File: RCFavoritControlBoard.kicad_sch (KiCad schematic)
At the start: 30 parts, among them J1 Screw_Terminal_01x02, J2 Screw_Terminal_01x02, J3 Conn_01x03_Pin, U1 SY8303, U2 TPS7A20xxxPDBVR, U3 DRV8833PWP, U4 XIAO-ESP32-S3-SMD

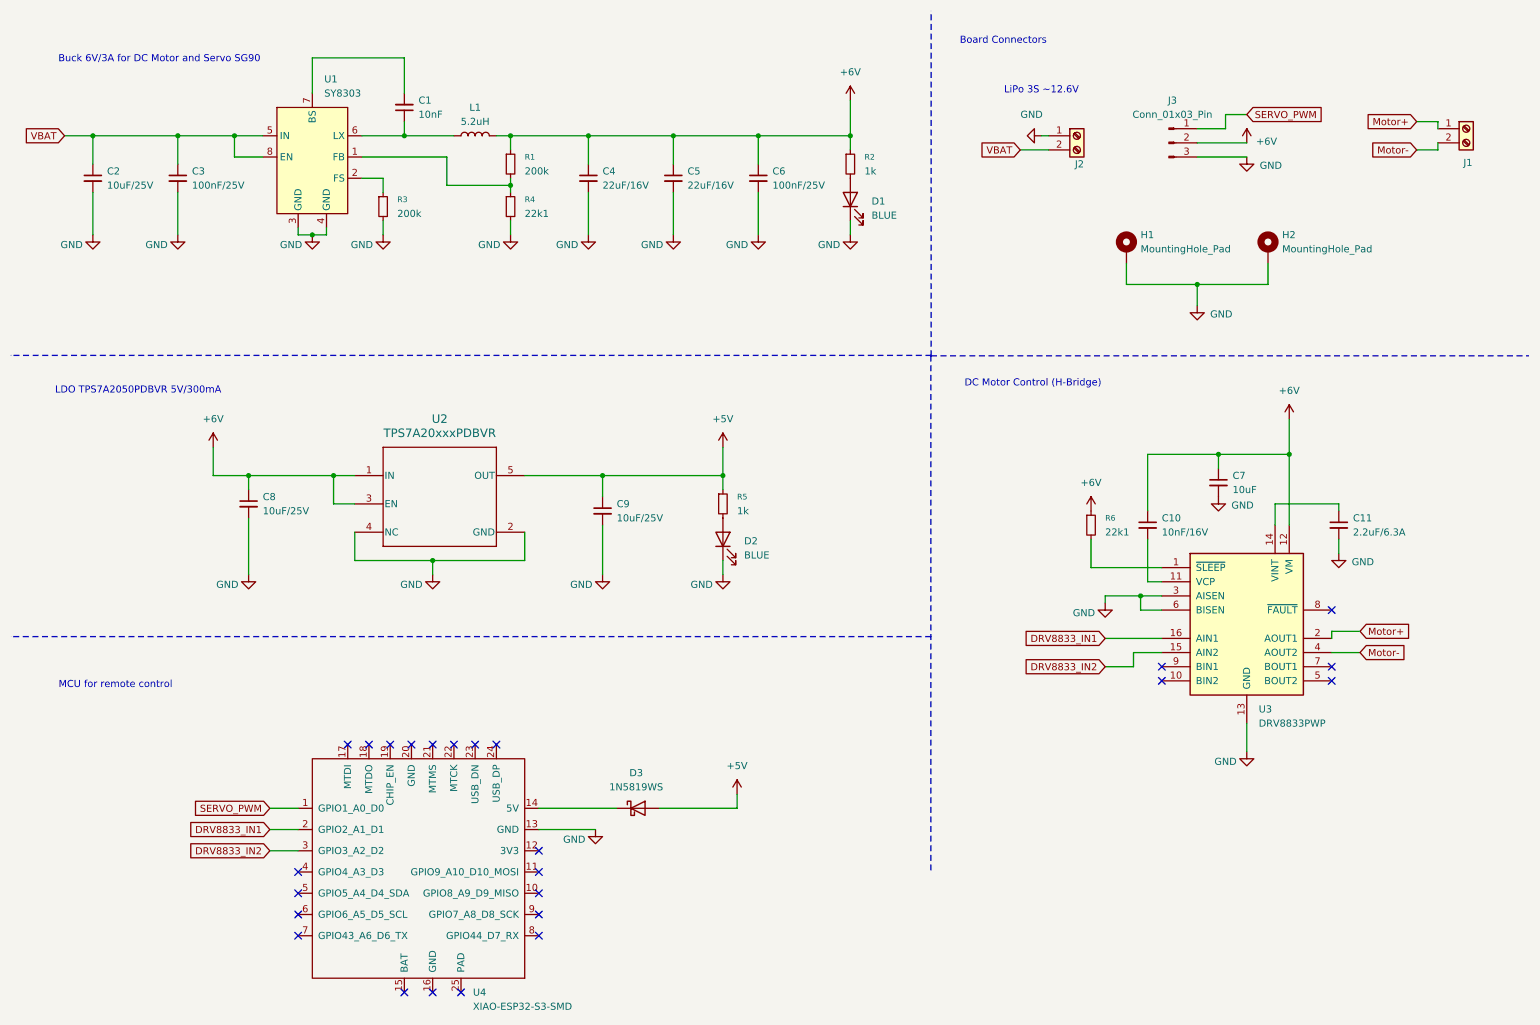
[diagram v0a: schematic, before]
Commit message: tried to use Fabrication Toolkit for JLCPCB
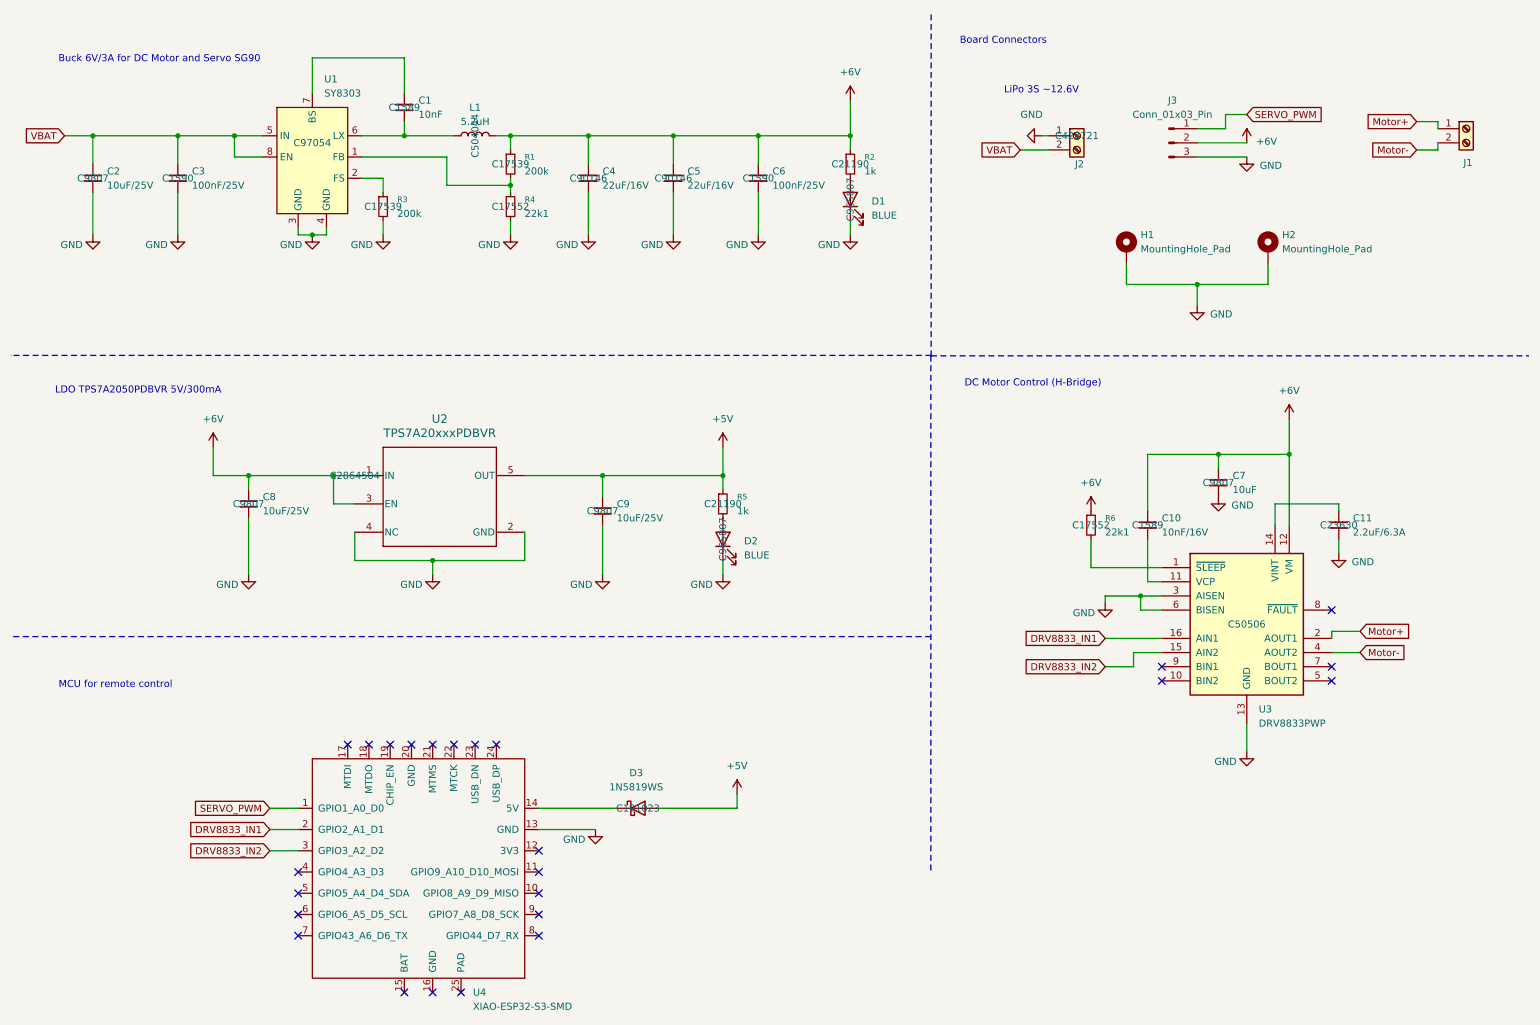
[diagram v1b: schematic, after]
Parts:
- C1, C10: LCSC Part # (none) -> C1589
- C11: LCSC Part # (none) -> C23630
- C2, C7, C8, C9: LCSC Part # (none) -> C9807
- C3, C6: LCSC Part # (none) -> C1590
- C4, C5: LCSC Part # (none) -> C90146
- D1, D2: LCSC Part # (none) -> C965807
- D3: LCSC Part # (none) -> C191023
- J1, J3, U4: now left out of the parts list
- J2: LCSC Part # (none) -> C428721
- L1: LCSC Part # (none) -> C504044
- R1, R3: LCSC Part # (none) -> C17539
- R2, R5: LCSC Part # (none) -> C21190
- R4, R6: LCSC Part # (none) -> C17552
- U1: LCSC Part # (none) -> C97054
- U2: LCSC Part # (none) -> C2864504
- U3: LCSC Part # (none) -> C50506
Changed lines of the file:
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@@
 			)
 		)
+		(property "LCSC Part #" "C90146"
+			(at 130.81 41.91 0)
+			(effects
+				(font
+					(size 1.27 1.27)
+				)
+			)
+		)
 		(pin "1"
 		)
@@
 			)
 		)
+		(property "LCSC Part #" "C17539"
+			(at 101.6 39.37 0)
+			(effects
+				(font
+					(size 1.27 1.27)
+				)
+			)
+		)
 		(pin "2"
 		)
@@
 			)
 		)
+		(property "LCSC Part #" "C9807"
+			(at 26.67 41.91 0)
+			(effects
+				(font
+					(size 1.27 1.27)
+				)
+			)
+		)
 		(pin "1"
 		)
@@
 		(unit 1)
 		(exclude_from_sim no)
-		(in_bom yes)
+		(in_bom no)
 		(on_board yes)
 		(dnp no)
@@
 			)
 		)
+		(property "LCSC Part #" "C504044"
+			(at 95.25 34.29 0)
+			(effects
+				(font
+					(size 1.27 1.27)
+				)
+			)
+		)
 		(pin "1"
 		)
@@
 			)
 		)
+		(property "LCSC Part #" "C9807"
+			(at 54.61 100.33 0)
+			(effects
+				(font
+					(size 1.27 1.27)
+				)
+			)
+		)
 		(pin "1"
 		)
@@
 			)
 		)
+		(property "LCSC Part #" "C17539"
+			(at 78.74 46.99 0)
+			(effects
+				(font
+					(size 1.27 1.27)
+				)
+			)
+		)
 		(pin "2"
 		)
@@
 		(unit 1)
 		(exclude_from_sim no)
-		(in_bom yes)
+		(in_bom no)
 		(on_board yes)
 		(dnp no)
@@
 			)
 		)
+		(property "LCSC Part #" "C428721"
+			(at 203.2 34.29 0)
+			(effects
+				(font
+					(size 1.27 1.27)
+				)
+			)
+		)
 		(pin "1"
 		)
@@
 			)
 		)
+		(property "LCSC Part #" "C21190"
+			(at 162.56 39.37 0)
+			(effects
+				(font
+					(size 1.27 1.27)
+				)
+			)
+		)
 		(pin "2"
 		)
@@
 			)
 		)
+		(property "LCSC Part #" "C1589"
+			(at 215.9 104.14 0)
+			(effects
+				(font
+					(size 1.27 1.27)
+				)
+			)
+		)
 		(pin "2"
 		)
@@
 			)
 		)
+		(property "LCSC Part #" "C9807"
+			(at 118.11 101.6 0)
+			(effects
+				(font
+					(size 1.27 1.27)
+				)
+			)
+		)
 		(pin "1"
 		)
@@
 			)
 		)
+		(property "LCSC Part #" "C2864504"
+			(at 73.66 95.25 0)
+			(effects
+				(font
+					(size 1.27 1.27)
+				)
+			)
+		)
 		(pin "5"
 		)
@@
 			)
 		)
+		(property "LCSC Part #" "C17552"
+			(at 101.6 46.99 0)
+			(effects
+				(font
+					(size 1.27 1.27)
+				)
+			)
+		)
 		(pin "2"
 		)
@@
 			)
 		)
+		(property "LCSC Part #" "C21190"
+			(at 139.7 100.33 0)
+			(effects
+				(font
+					(size 1.27 1.27)
+				)
+			)
+		)
 		(pin "2"
 		)
@@
 			)
 		)
+		(property "LCSC Part #" "C90146"
+			(at 115.57 41.91 0)
+			(effects
+				(font
+					(size 1.27 1.27)
+				)
+			)
+		)
 		(pin "1"
 		)
@@
 			)
 		)
+		(property "LCSC Part #" "C9807"
+			(at 228.6 96.52 0)
+			(effects
+				(font
+					(size 1.27 1.27)
+				)
+			)
+		)
 		(pin "2"
 		)
@@
 			)
 		)
+		(property "LCSC Part #" "C191023"
+			(at 124.46 154.94 0)
+			(effects
+				(font
+					(size 1.27 1.27)
+				)
+			)
+		)
 		(pin "1"
 		)
@@
 			)
 		)
+		(property "LCSC Part #" "C97054"
+			(at 66.04 35.56 0)
+			(effects
+				(font
+					(size 1.27 1.27)
+				)
+			)
+		)
 		(pin "3"
 		)
@@
 		(unit 1)
 		(exclude_from_sim no)
-		(in_bom yes)
+		(in_bom no)
 		(on_board yes)
 		(dnp no)
@@
 			)
 		)
+		(property "LCSC Part #" "C50506"
+			(at 233.68 121.92 0)
+			(effects
+				(font
+					(size 1.27 1.27)
+				)
+			)
+		)
 		(pin "15"
 		)
@@
 			)
 		)
+		(property "LCSC Part #" "C965807"
+			(at 139.7 106.68 0)
+			(effects
+				(font
+					(size 1.27 1.27)
+				)
+			)
+		)
 		(pin "2"
 		)
@@
 			)
 		)
+		(property "LCSC Part #" "C23630"
+			(at 250.19 104.14 0)
+			(effects
+				(font
+					(size 1.27 1.27)
+				)
+			)
+		)
 		(pin "2"
 		)
@@
 			)
 		)
+		(property "LCSC Part #" "C1590"
+			(at 146.05 41.91 0)
+			(effects
+				(font
+					(size 1.27 1.27)
+				)
+			)
+		)
 		(pin "1"
 		)
@@
 			)
 		)
+		(property "LCSC Part #" " C1589"
+			(at 82.55 29.21 0)
+			(effects
+				(font
+					(size 1.27 1.27)
+				)
+			)
+		)
 		(pin "1"
 		)
@@
 			)
 		)
+		(property "LCSC Part #" "C965807"
+			(at 162.56 45.72 0)
+			(effects
+				(font
+					(size 1.27 1.27)
+				)
+			)
+		)
 		(pin "2"
 		)
@@
 			)
 		)
+		(property "LCSC Part #" "C17552"
+			(at 205.74 104.14 0)
+			(effects
+				(font
+					(size 1.27 1.27)
+				)
+			)
+		)
 		(pin "2"
 		)
@@
 			)
 		)
+		(property "LCSC Part #" "C1590"
+			(at 41.91 41.91 0)
+			(effects
+				(font
+					(size 1.27 1.27)
+				)
+			)
+		)
